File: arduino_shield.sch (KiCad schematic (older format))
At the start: 1 part

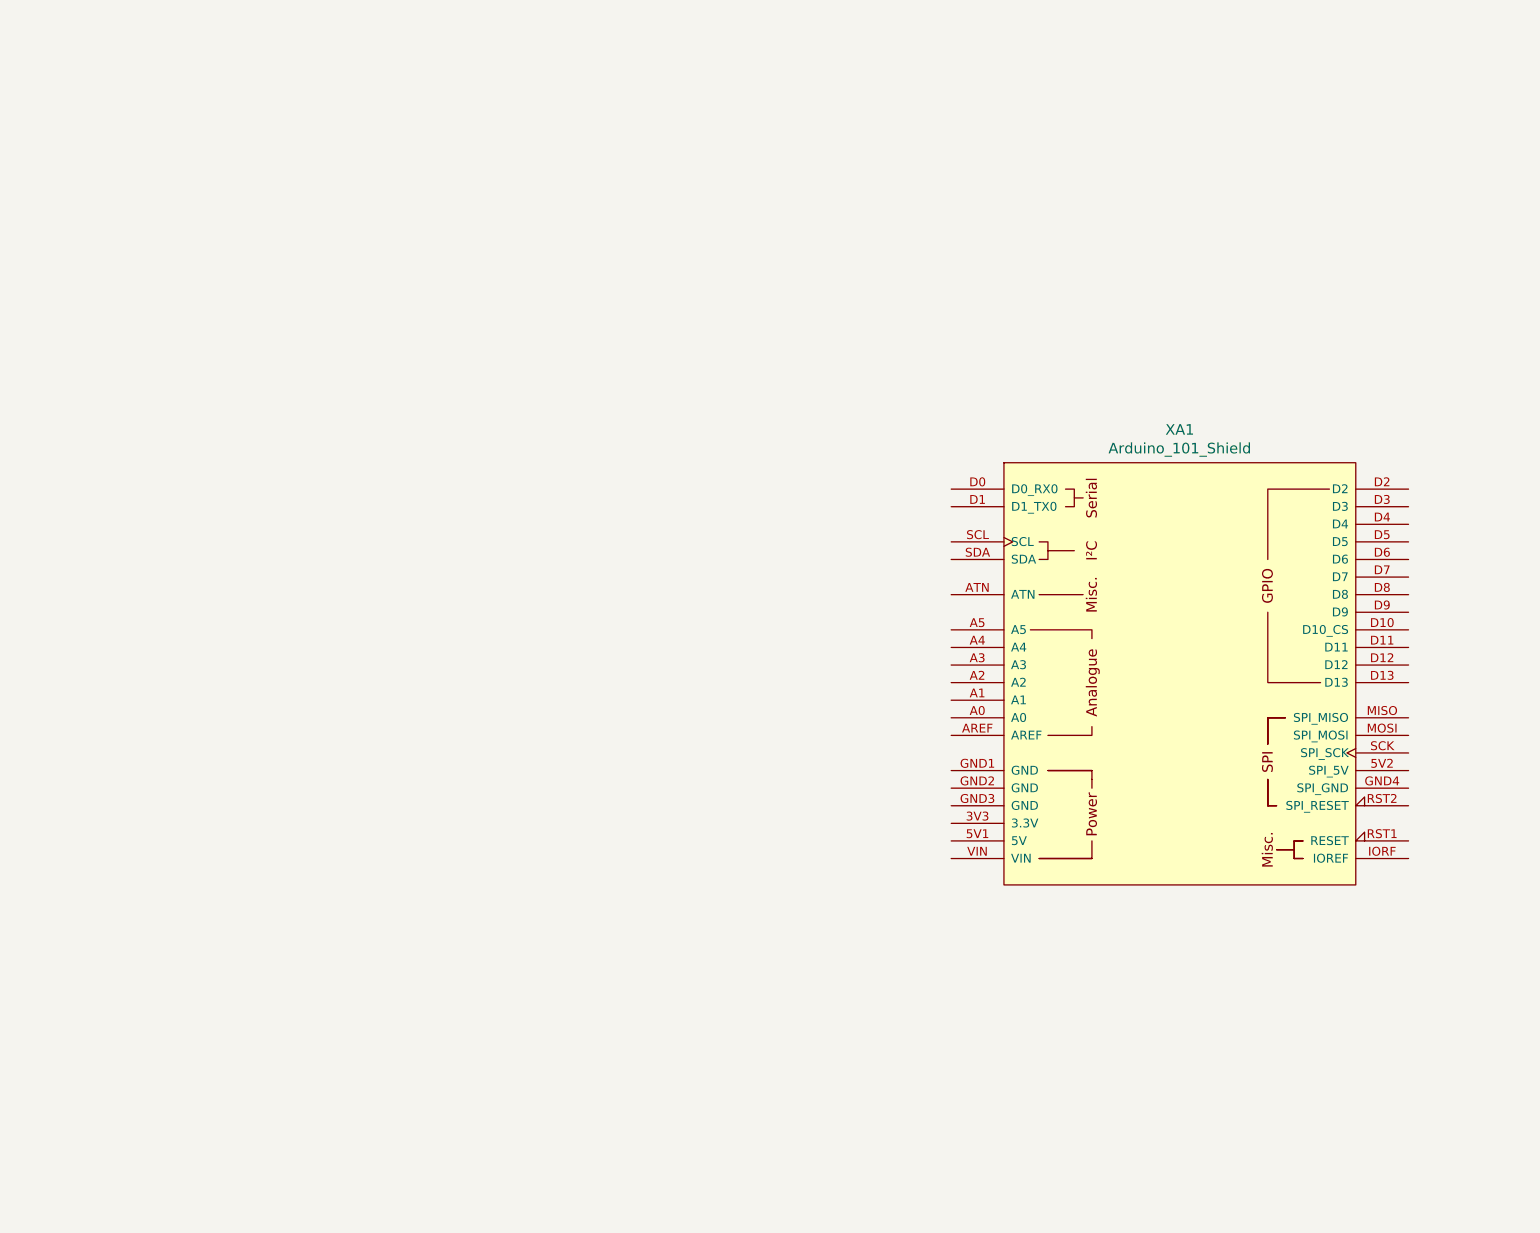
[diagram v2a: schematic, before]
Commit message: Updated schematic, added some components, figurated components on pcb
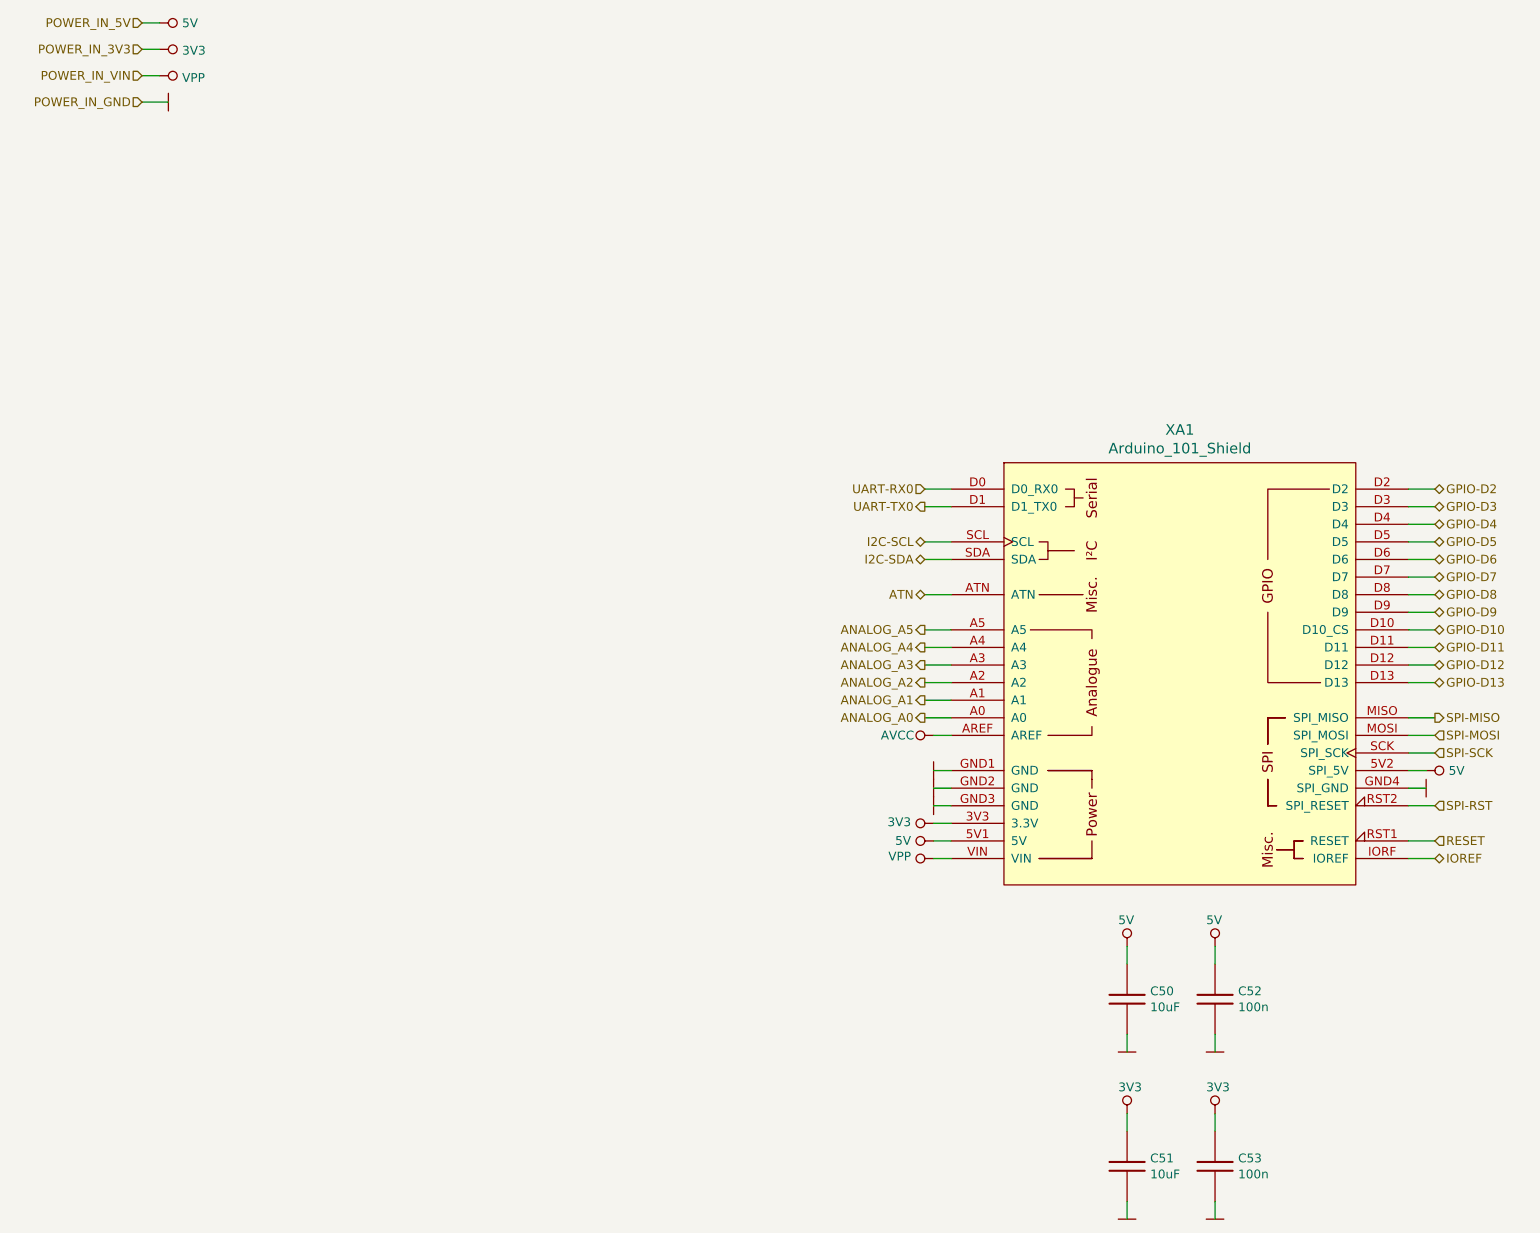
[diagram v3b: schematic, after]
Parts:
- added C50, C51: 10uF, Capacitors_Smd_0603:10uF_10V_0603, symbol Capacitors_Smd0603:10uF
- added C52, C53: 100n, Capacitors_Smd_0603:100nF_0603, symbol Capacitors_Smd0603:100n
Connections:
- net 3V3: now reaches XA1.3V3 (3.3V)
- net 3V3: now also C51.1, C53.1
- net 5V: now reaches XA1.5V1 (5V)
- net 5V: now also XA1.5V2 (SPI_5V), C50.1, C52.1
- net ANALOG_A0: now reaches XA1.A0
- net ANALOG_A1: now reaches XA1.A1
- net ANALOG_A2: now reaches XA1.A2
- net ANALOG_A3: now reaches XA1.A3
- net ANALOG_A4: now reaches XA1.A4
- net ANALOG_A5: now reaches XA1.A5
- net VCC-RTC: now reaches XA1.AREF
- net ATN: now reaches XA1.ATN
- net UART-RX0: now reaches XA1.D0 (D0_RX0)
- net UART-TX0: now reaches XA1.D1 (D1_TX0)
- net GPIO-D10: now reaches XA1.D10 (D10_CS)
- net GPIO-D11: now reaches XA1.D11
- net GPIO-D12: now reaches XA1.D12
- net GPIO-D13: now reaches XA1.D13
- net GPIO-D2: now reaches XA1.D2
- net GPIO-D3: now reaches XA1.D3
- net GPIO-D4: now reaches XA1.D4
- net GPIO-D5: now reaches XA1.D5
- net GPIO-D6: now reaches XA1.D6
- net GPIO-D7: now reaches XA1.D7
- net GPIO-D8: now reaches XA1.D8
- net GPIO-D9: now reaches XA1.D9
- net GND: now reaches XA1.GND1 (GND)
- net GND: now also XA1.GND2 (GND), XA1.GND3 (GND), XA1.GND4 (SPI_GND), C50.2, C51.2, C52.2, C53.2
- net IOREF: now reaches XA1.IORF (IOREF)
- net SPI-MISO: now reaches XA1.MISO (SPI_MISO)
- net SPI-MOSI: now reaches XA1.MOSI (SPI_MOSI)
- net RESET: now reaches XA1.RST1 (RESET)
- net SPI-RST: now reaches XA1.RST2 (SPI_RESET)
- net SPI-SCK: now reaches XA1.SCK (SPI_SCK)
- net I2C-SCL: now reaches XA1.SCL
- net I2C-SDA: now reaches XA1.SDA
- net VPP: now reaches XA1.VIN

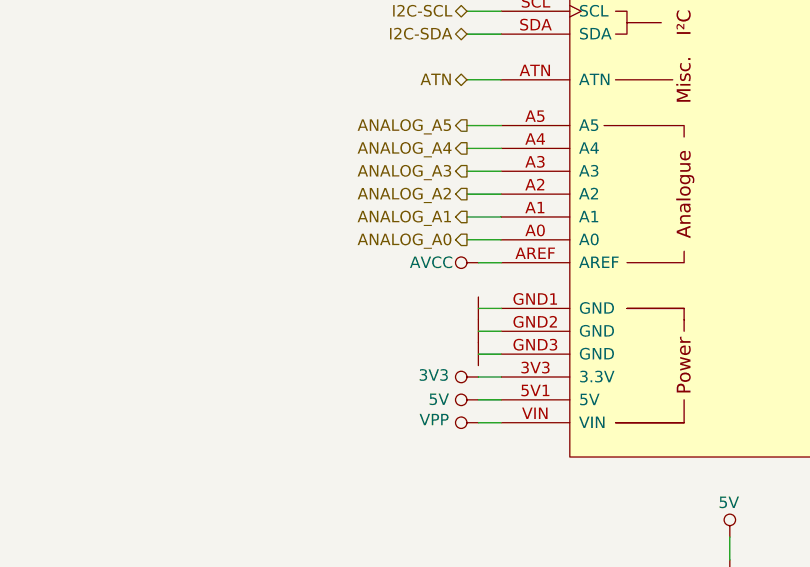
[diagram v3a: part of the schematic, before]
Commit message: Tracking finished, started tunning
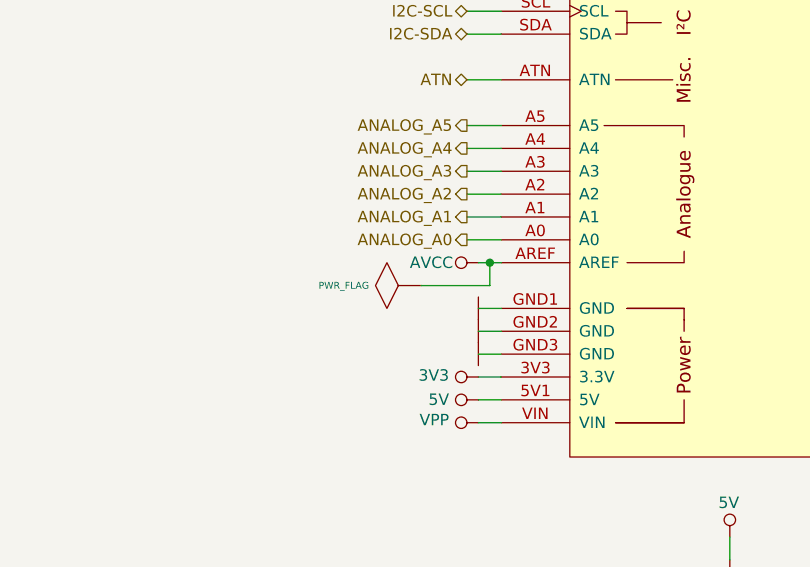
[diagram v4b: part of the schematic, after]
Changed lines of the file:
@@
 $EndComp
 Wire Wire Line
-	6850 5900 6750 5900
+	6850 5900 6800 5900
 $Comp
 L power:5V_NO_GLOBAL #PWR?
@@
 Text HLabel 9600 6500 2    50   Input ~ 0
 RESET
-Wire Wire Line
-	9450 6500 9600 6500
 Text HLabel 9600 6600 2    50   BiDi ~ 0
 IOREF
@@
 	1    0    0    -1
 $EndComp
+$Comp
+L power:PWR_FLAG #FLG0105
+U 1 1 600B3178
+P 6500 6000
+F 0 "#FLG0105" H 6500 6270 30  0001 C CNN
+F 1 "PWR_FLAG" V 6500 6228 30  0000 L CNN
+F 2 "" H 6500 6000 60  0000 C CNN
+F 3 "" H 6500 6000 60  0000 C CNN
+	1    6500 6000
+	0    -1   -1   0
+$EndComp
+Wire Wire Line
+	6800 5900 6800 6000
+Wire Wire Line
+	6800 6000 6500 6000
+Connection ~ 6800 5900
+Wire Wire Line
+	6800 5900 6750 5900
+Wire Wire Line
+	9450 6500 9600 6500
 $EndSCHEMATC

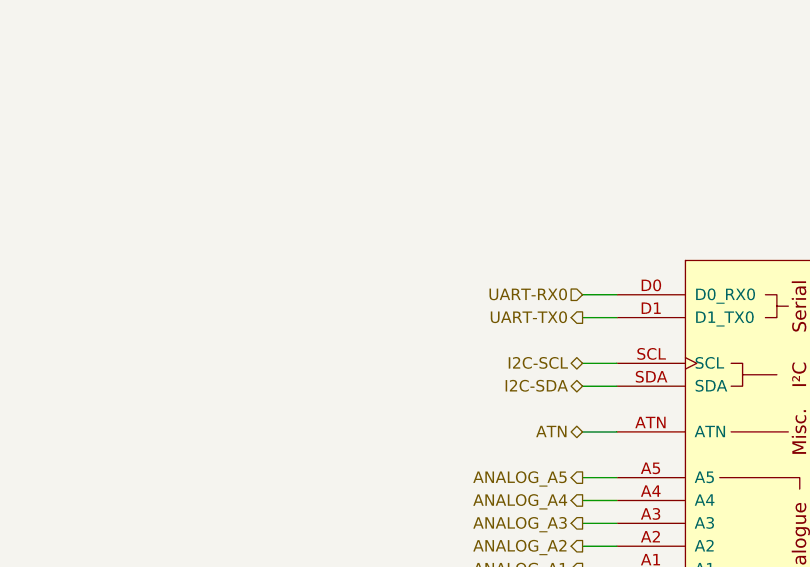
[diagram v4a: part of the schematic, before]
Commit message: Added missing components like LED diodes, i2c pull-up resistors
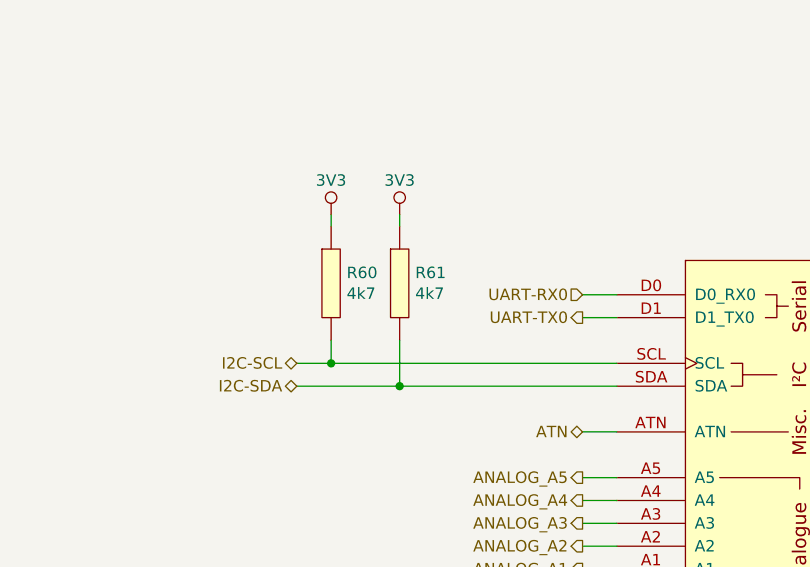
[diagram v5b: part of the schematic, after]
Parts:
- added R60, R61: 4k7, Resistor_Smd_0603:4k7_0603, symbol Resistors_Smd0603:4k7
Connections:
- net 3V3: now also R60.1, R61.1
- net I2C-SCL: now also R60.2
- net I2C-SDA: now also R61.2
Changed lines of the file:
@@
 Wire Wire Line
 	6850 5100 6700 5100
-Text HLabel 6700 4900 0    50   BiDi ~ 0
+Text HLabel 5450 4900 0    50   BiDi ~ 0
 I2C-SDA
-Text HLabel 6700 4800 0    50   BiDi ~ 0
+Text HLabel 5450 4800 0    50   BiDi ~ 0
 I2C-SCL
 Wire Wire Line
-	6850 4900 6700 4900
-Wire Wire Line
-	6850 4800 6700 4800
+	6850 4900 5900 4900
+Wire Wire Line
+	6850 4800 5600 4800
 Text HLabel 6700 4600 0    50   Output ~ 0
 UART-TX0
@@
 Wire Wire Line
 	9450 6500 9600 6500
+$Comp
+L Resistors_Smd0603:4k7 R?
+U 1 1 60123023
+P 5600 4450
+AR Path="/5FDE4F7C/60123023" Ref="R?"  Part="1"
+AR Path="/5FFEC95A/60123023" Ref="R?"  Part="1"
+AR Path="/60087A46/60123023" Ref="R60"  Part="1"
+F 0 "R60" H 5668 4496 50  0000 L CNN
+F 1 "4k7" H 5668 4405 50  0000 L CNN
+F 2 "Resistor_Smd_0603:4k7_0603" H 5600 4450 50  0001 C CNN
+F 3 "Resistors/Smd_0603/Components_Documentation/Vishay_Resistors_SM0603.pdf" H 5600 4450 50  0001 C CNN
+F 4 "ROYAL OHM" H 5600 4450 50  0001 C CNN "Manufacturer"
+F 5 "0603SAF4701T5E" H 5600 4450 50  0001 C CNN "Manufacturer Part Number"
+F 6 "TME" H 5600 4450 50  0001 C CNN "Supplier"
+F 7 "	SMD0603-4K7-1%" H 5600 4450 50  0001 C CNN "Supplier Part Number"
+F 8 "https://www.tme.eu/pl/details/smd0603-4k7-1%2525/rezystory-smd-0603/royal-ohm/0603saf4701t5e/" H 5600 4450 50  0001 C CNN "URL"
+F 9 "0,04698" H 5600 4450 50  0001 C CNN "Price@1pc"
+F 10 "0,01271" H 5600 4450 50  0001 C CNN "Price@1000pcs"
+F 11 "0603" H 5600 4450 50  0001 C CNN "Package"
+	1    5600 4450
+	1    0    0    -1
+$EndComp
+$Comp
+L power:3V3_NO_GLOBAL #PWR?
+U 1 1 60123029
+P 5600 4150
+AR Path="/5FDE4F7C/60123029" Ref="#PWR?"  Part="1"
+AR Path="/5FFEC95A/60123029" Ref="#PWR?"  Part="1"
+AR Path="/60087A46/60123029" Ref="#PWR201"  Part="1"
+F 0 "#PWR201" H 5600 4250 40  0001 C CNN
+F 1 "3V3" H 5600 4300 50  0000 C CNN
+F 2 "" H 5600 4150 60  0000 C CNN
+F 3 "" H 5600 4150 60  0000 C CNN
+	1    5600 4150
+	1    0    0    -1
+$EndComp
+Wire Wire Line
+	5600 4150 5600 4200
+$Comp
+L Resistors_Smd0603:4k7 R?
+U 1 1 60123038
+P 5900 4450
+AR Path="/5FDE4F7C/60123038" Ref="R?"  Part="1"
+AR Path="/5FFEC95A/60123038" Ref="R?"  Part="1"
+AR Path="/60087A46/60123038" Ref="R61"  Part="1"
+F 0 "R61" H 5968 4496 50  0000 L CNN
+F 1 "4k7" H 5968 4405 50  0000 L CNN
+F 2 "Resistor_Smd_0603:4k7_0603" H 5900 4450 50  0001 C CNN
+F 3 "Resistors/Smd_0603/Components_Documentation/Vishay_Resistors_SM0603.pdf" H 5900 4450 50  0001 C CNN
+F 4 "ROYAL OHM" H 5900 4450 50  0001 C CNN "Manufacturer"
+F 5 "0603SAF4701T5E" H 5900 4450 50  0001 C CNN "Manufacturer Part Number"
+F 6 "TME" H 5900 4450 50  0001 C CNN "Supplier"
+F 7 "	SMD0603-4K7-1%" H 5900 4450 50  0001 C CNN "Supplier Part Number"
+F 8 "https://www.tme.eu/pl/details/smd0603-4k7-1%2525/rezystory-smd-0603/royal-ohm/0603saf4701t5e/" H 5900 4450 50  0001 C CNN "URL"
+F 9 "0,04698" H 5900 4450 50  0001 C CNN "Price@1pc"
+F 10 "0,01271" H 5900 4450 50  0001 C CNN "Price@1000pcs"
+F 11 "0603" H 5900 4450 50  0001 C CNN "Package"
+	1    5900 4450
+	1    0    0    -1
+$EndComp
+$Comp
+L power:3V3_NO_GLOBAL #PWR?
+U 1 1 6012303E
+P 5900 4150
+AR Path="/5FDE4F7C/6012303E" Ref="#PWR?"  Part="1"
+AR Path="/5FFEC95A/6012303E" Ref="#PWR?"  Part="1"
+AR Path="/60087A46/6012303E" Ref="#PWR202"  Part="1"
+F 0 "#PWR202" H 5900 4250 40  0001 C CNN
+F 1 "3V3" H 5900 4300 50  0000 C CNN
+F 2 "" H 5900 4150 60  0000 C CNN
+F 3 "" H 5900 4150 60  0000 C CNN
+	1    5900 4150
+	1    0    0    -1
+$EndComp
+Wire Wire Line
+	5900 4150 5900 4200
+Wire Wire Line
+	5900 4700 5900 4900
+Connection ~ 5900 4900
+Wire Wire Line
+	5900 4900 5450 4900
+Wire Wire Line
+	5600 4700 5600 4800
+Connection ~ 5600 4800
+Wire Wire Line
+	5600 4800 5450 4800
 $EndSCHEMATC
